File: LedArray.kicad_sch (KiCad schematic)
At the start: 32 parts

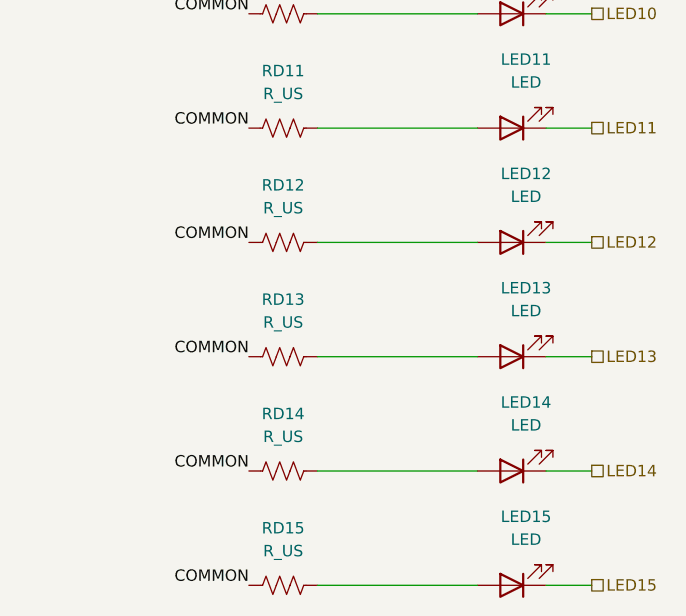
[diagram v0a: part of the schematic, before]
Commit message: Swap LED controller for TLC5971
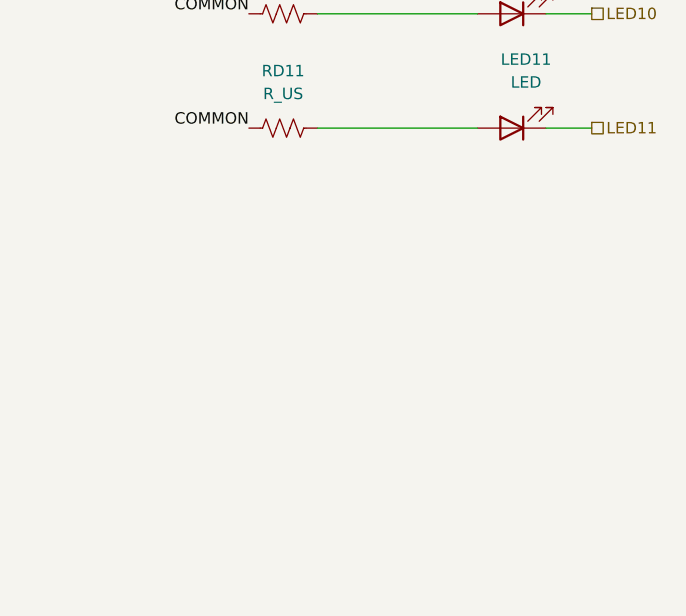
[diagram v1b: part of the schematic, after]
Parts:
- removed LED12, LED13, LED14, LED15: LED, LED_SMD:LED_Cree-XP-G, symbol Device:LED
- removed RD12, RD13, RD14, RD15: R_US, Resistor_SMD:R_1206_3216Metric, symbol Device:R_US
